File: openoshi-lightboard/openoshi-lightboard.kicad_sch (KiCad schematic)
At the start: 28 parts, among them J1 USB_C_Receptacle_PowerOnly_6P, Q1 CSD17484F4, Q2 CSD17484F4, Q3 CSD17484F4, Q4 CSD17484F4, SW1 SW_Push, SW2 SW_Push, U1 CH32V003FxUx, U2 TLV61220, U3 MCP73831-2-OT

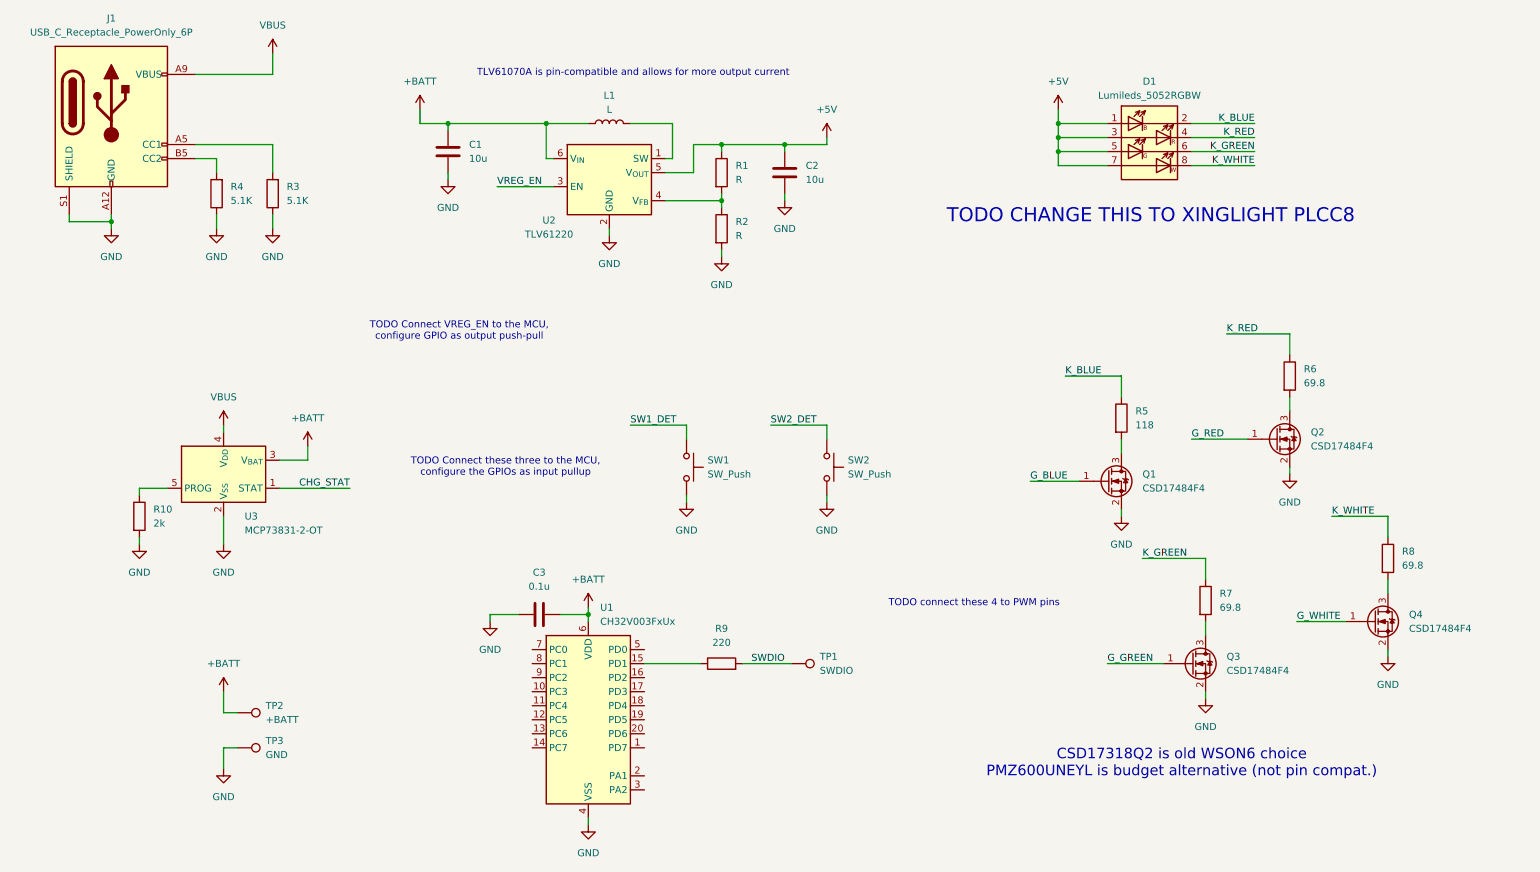
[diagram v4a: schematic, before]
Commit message: Tentative sch completion, initial layout
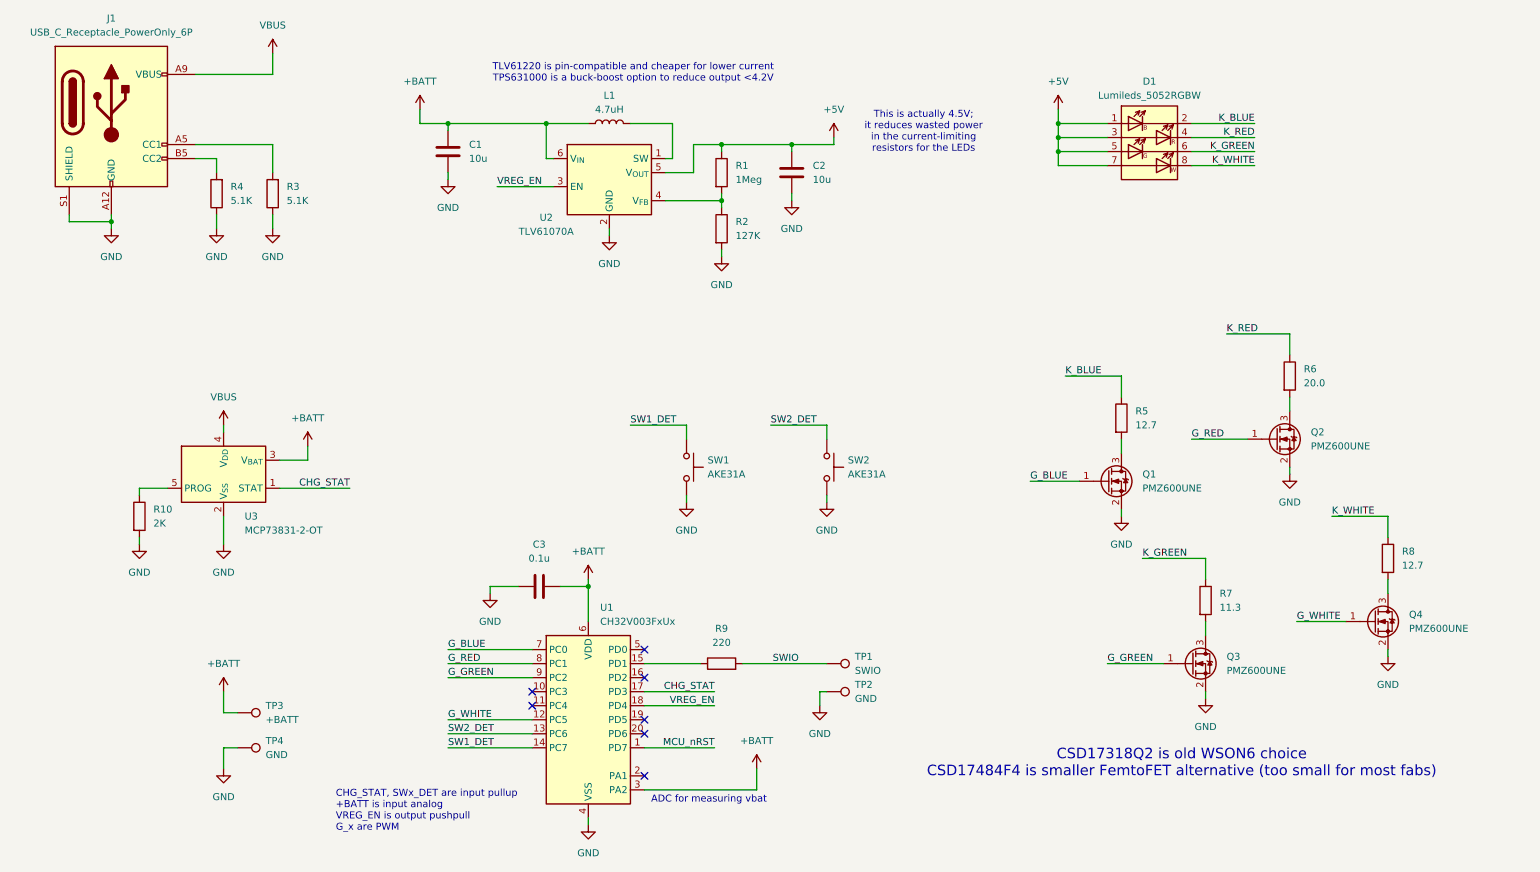
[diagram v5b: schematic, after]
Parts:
- removed Q1, Q2, Q3, Q4: CSD17484F4, Package_DFN_QFN:Texas_PicoStar_DFN-3_0.69x0.60mm, symbol Transistor_FET:CSD13380F3
- added Q1, Q2, Q3, Q4: PMZ600UNE, Package_TO_SOT_SMD:SOT-883, symbol openoshi-lightboard:PMZ600UNE
- added TP2: GND, TestPoint:TestPoint_Pad_D1.0mm, symbol Connector:TestPoint
- L1: value L -> 4.7uH
- R1: value R -> 1Meg
- R10: value 2k -> 2K
- R2: value R -> 127K
- R5: value 118 -> 12.7
- R6: value 69.8 -> 20.0
- R7: value 69.8 -> 11.3
- R8: value 69.8 -> 12.7
- SW1, SW2: value SW_Push -> AKE31A
- TP1: value SWDIO -> SWIO; footprint TestPoint:TestPoint_Pad_D1.5mm -> TestPoint:TestPoint_Pad_D1.0mm
- U2: value TLV61220 -> TLV61070A
- renumbered TP2 to TP3, TP3 to TP4
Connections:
- net +BATT: now also U1.3 (PA2)
- net CHG_STAT: now also U1.17 (PD3)
- net GND: now also Q1.2 (S), Q2.2 (S), Q3.2 (S), Q4.2 (S), TP2.1
- net G_BLUE: now also U1.7 (PC0), Q1.1 (G)
- net G_GREEN: now also U1.9 (PC2), Q3.1 (G)
- net G_RED: now also U1.8 (PC1), Q2.1 (G)
- net G_WHITE: now also U1.12 (PC5), Q4.1 (G)
- net SW1_DET: now also U1.14 (PC7)
- net SW2_DET: now also U1.13 (PC6)
- net VREG_EN: now also U1.18 (PD4)
- net at R8.2: now also Q4.3 (D)
- net at R5.2: now also Q1.3 (D)
- net at R6.2: now also Q2.3 (D)
- net at R7.2: now also Q3.3 (D)
- net MCU_nRST: now reaches U1.1 (PD7)
- net SWDIO renamed SWIO
- no-connect marks 0 -> 7
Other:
- note added: "ADC for measuring vbat"
- note added: "CHG_STAT, SWx_DET are input pullup +BATT is input analog VREG_EN is output pushpull G_x are PWM"
- note added: "CSD17318Q2 is old WSON6 choice CSD17484F4 is smaller FemtoFET alternative (too small for most fabs)"
- note added: "TLV61220 is pin-compatible and cheaper for lower current TPS631000 is a buck-boost option to reduce output <4.2V"
- note added: "This is actually 4.5V; it reduces wasted power in the current-limiting resistors for the LEDs"
- note removed: "CSD17318Q2 is old WSON6 choice PMZ600UNEYL is budget alternative (not pin compat.)"
- note removed: "TLV61070A is pin-compatible and allows for more output current"
- note removed: "TODO CHANGE THIS TO XINGLIGHT PLCC8"
- note removed: "TODO Connect VREG_EN to the MCU, configure GPIO as output push-pull"
- note removed: "TODO Connect these three to the MCU, configure the GPIOs as input pullup"
- note removed: "TODO connect these 4 to PWM pins"
- moved on the sheet: C2, C3

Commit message: Reroute complete
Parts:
- R5, R6, R7, R8: footprint Resistor_SMD:R_0603_1608Metric -> Resistor_SMD:R_1206_3216Metric
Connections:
- net CHG_STAT: now also U1.2 (PA1); no longer U1.17 (PD3)
- net G_BLUE: now also U1.11 (PC4); no longer U1.7 (PC0)
- net G_GREEN: now also U1.14 (PC7); no longer U1.9 (PC2)
- net G_RED: now also U1.12 (PC5); no longer U1.8 (PC1)
- net G_WHITE: now also U1.18 (PD4); no longer U1.12 (PC5)
- net SW1_DET: now also U1.20 (PD6); no longer U1.14 (PC7)
- net SW2_DET: now also U1.19 (PD5); no longer U1.13 (PC6)
- net VREG_EN: now also U1.10 (PC3); no longer U1.18 (PD4)
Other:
- note added: "CHG_STAT, SWx_DET are input pullup +BATT is input analog (AIN0) VREG_EN is output pushpull G_x are PWM (TIM1_RM=11)"
- note removed: "CHG_STAT, SWx_DET are input pullup +BATT is input analog VREG_EN is output pushpull G_x are PWM"

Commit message: Assembly files created, first run
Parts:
- TP3, TP4: footprint TestPoint:TestPoint_Keystone_5019_Miniature -> openoshi-lightboard:Battery_SolderPad
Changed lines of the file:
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@@
 			)
 		)
-		(property "Footprint" "TestPoint:TestPoint_Keystone_5019_Miniature"
+		(property "Footprint" "openoshi-lightboard:Battery_SolderPad"
 			(at 57.15 161.29 0)
 			(effects
@@
 			)
 		)
-		(property "Footprint" "TestPoint:TestPoint_Keystone_5019_Miniature"
+		(property "Footprint" "openoshi-lightboard:Battery_SolderPad"
 			(at 57.15 154.94 0)
 			(effects

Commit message: Begin firmware work
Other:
- note added: "TIM1_CH1"
- note added: "TIM1_CH2"
- note added: "TIM1_CH3"
- note added: "TIM1_CH4"
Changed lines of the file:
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@@
 	(generator_version "9.0")
 	(paper "A4")
+	(text "TIM1_CH3"
+		(exclude_from_sim no)
+		(at 89.154 150.622 0)
+		(effects
+			(font
+				(size 1.27 1.27)
+			)
+		)
+	)
 	(text "This is actually 4.5V;\nit reduces wasted power\nin the current-limiting\nresistors for the LEDs"
 		(exclude_from_sim no)
 		(at 181.356 44.704 0)
+		(effects
+			(font
+				(size 1.27 1.27)
+			)
+		)
+	)
+	(text "TIM1_CH2"
+		(exclude_from_sim no)
+		(at 89.154 155.702 0)
 		(effects
 			(font
@@
 			)
 		)
+	)
+	(text "TIM1_CH1"
+		(exclude_from_sim no)
+		(at 89.154 148.082 0)
+		(effects
+			(font
+				(size 1.27 1.27)
+			)
+		)
+	)
+	(text "TIM1_CH4"
+		(exclude_from_sim no)
+		(at 149.352 147.828 0)
+		(effects
+			(font
+				(size 1.27 1.27)
+			)
+		)
